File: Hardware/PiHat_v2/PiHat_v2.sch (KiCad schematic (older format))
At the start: 35 parts, among them P1 RPiGPIO, P2 CONN_01X02, P3 CONN_01X08

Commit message: KiCad Closeout Updates
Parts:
- renumbered aux1 to ADC6, aux3 to GPIO20, aux4 to GPIO21, aux5 to GPIO26, S1 to PB1, aux2 to PD3
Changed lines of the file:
@@
 $EndComp
 $Comp
-L Piezo S1
+L Piezo PB1
 U 1 1 5889681E
 P 6000 5100
-F 0 "S1" H 6000 5250 50  0000 C CNN
+F 0 "PB1" H 6000 5250 50  0000 C CNN
 F 1 "Piezo" V 6100 5100 50  0000 C CNN
 F 2 ".pretty:Piezo_CT-1205h-smt" H 6000 5100 50  0001 C CNN
@@
 	4450 1050 4450 1250
 $Comp
-L aux_conn aux1
+L aux_conn ADC6
 U 1 1 5946D2A9
 P 6050 5850
-F 0 "aux1" H 6050 6000 50  0000 C CNN
+F 0 "ADC6" H 6050 6000 50  0000 C CNN
 F 1 "aux_conn" V 6150 5850 50  0000 C CNN
 F 2 ".pretty:Pin_Header_Straight_1x02_Pitch2.54mm" H 6050 5850 50  0001 C CNN
@@
 $EndComp
 $Comp
-L aux_conn aux2
+L aux_conn PD3
 U 1 1 5946D408
 P 6050 6200
-F 0 "aux2" H 6050 6350 50  0000 C CNN
+F 0 "PD3" H 6050 6350 50  0000 C CNN
 F 1 "aux_conn" V 6150 6200 50  0000 C CNN
 F 2 ".pretty:Pin_Header_Straight_1x02_Pitch2.54mm" H 6050 6200 50  0001 C CNN
@@
 $EndComp
 $Comp
-L aux_conn aux3
+L aux_conn GPIO20
 U 1 1 5946D47A
 P 6050 6550
-F 0 "aux3" H 6050 6700 50  0000 C CNN
+F 0 "GPIO20" H 6050 6700 50  0000 C CNN
 F 1 "aux_conn" V 6150 6550 50  0000 C CNN
 F 2 ".pretty:Pin_Header_Straight_1x02_Pitch2.54mm" H 6050 6550 50  0001 C CNN
@@
 $EndComp
 $Comp
-L aux_conn aux4
+L aux_conn GPIO21
 U 1 1 5946D4EB
 P 6050 6900
-F 0 "aux4" H 6050 7050 50  0000 C CNN
+F 0 "GPIO21" H 6050 7050 50  0000 C CNN
 F 1 "aux_conn" V 6150 6900 50  0000 C CNN
 F 2 ".pretty:Pin_Header_Straight_1x02_Pitch2.54mm" H 6050 6900 50  0001 C CNN
@@
 $EndComp
 $Comp
-L aux_conn aux5
+L aux_conn GPIO26
 U 1 1 5946D55F
 P 6050 7250
-F 0 "aux5" H 6050 7400 50  0000 C CNN
+F 0 "GPIO26" H 6050 7400 50  0000 C CNN
 F 1 "aux_conn" V 6150 7250 50  0000 C CNN
 F 2 ".pretty:Pin_Header_Straight_1x02_Pitch2.54mm" H 6050 7250 50  0001 C CNN

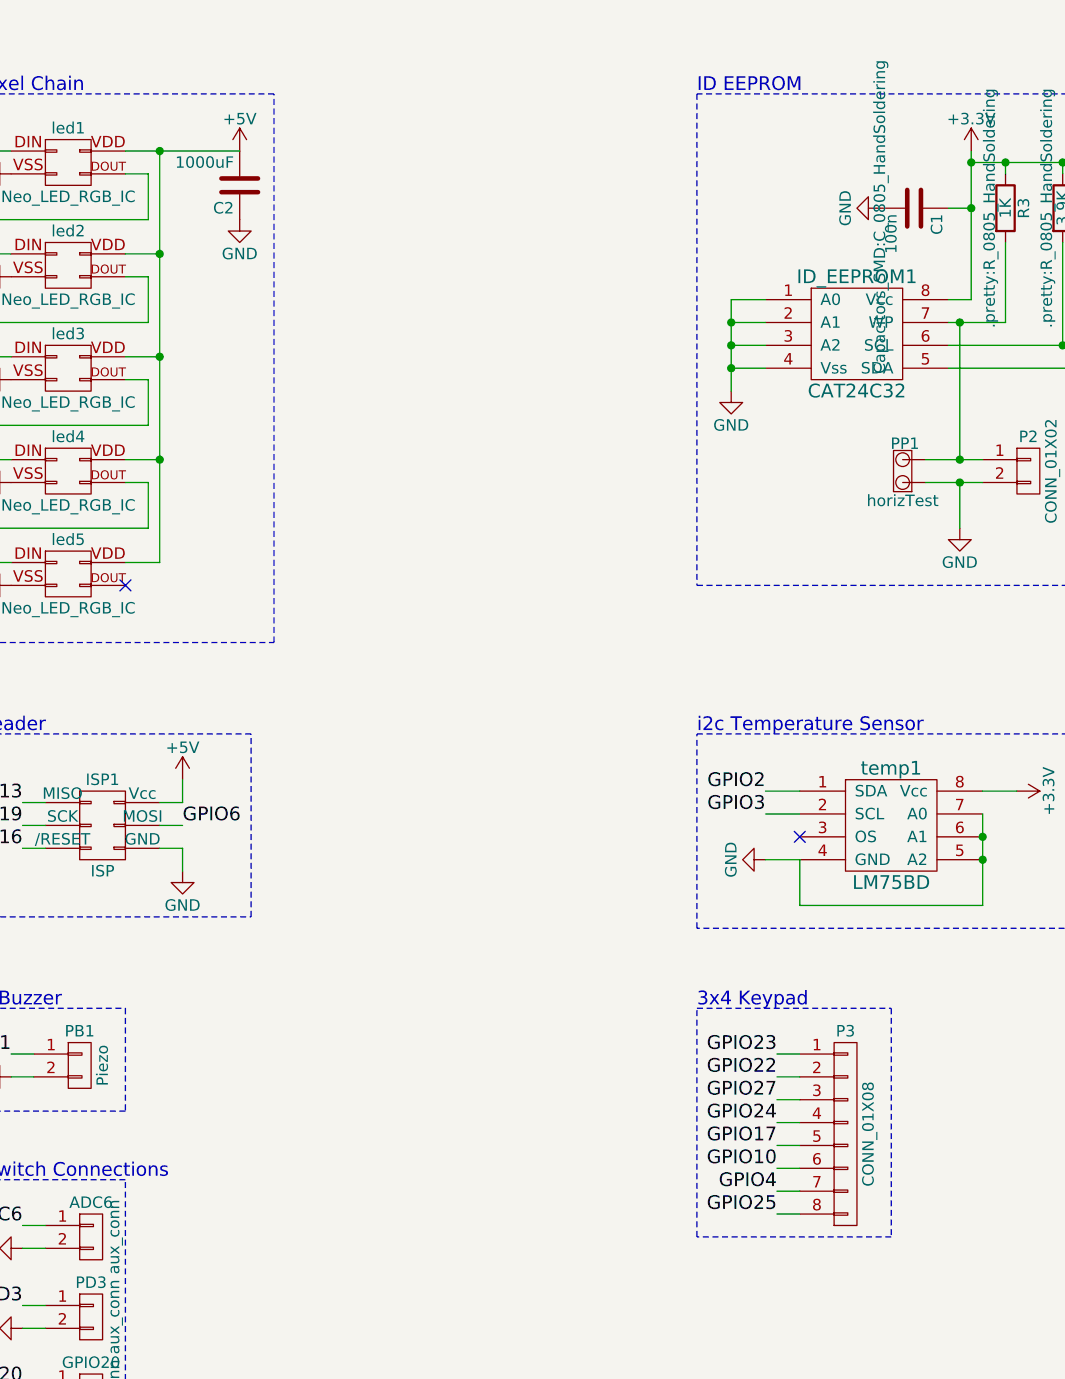
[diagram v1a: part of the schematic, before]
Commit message: Pi Hat - now with non-imaginary components (#155)
* Adjust Silkscreen Layout on PCB

* Add 1000uF AluCap Footprint & Rename 100nF to 0.1uF

* Implement AluCap in PCB

* Connect New Keypad GPIO Schema

* Built the BOM

* Move Silkscreen Logo

* YASA - Yet Another Silkscreen Adjustment

* Update Version Number of PiHat

* Rotate AluCap for Proper Polarity

* Fix BOM Whitespace
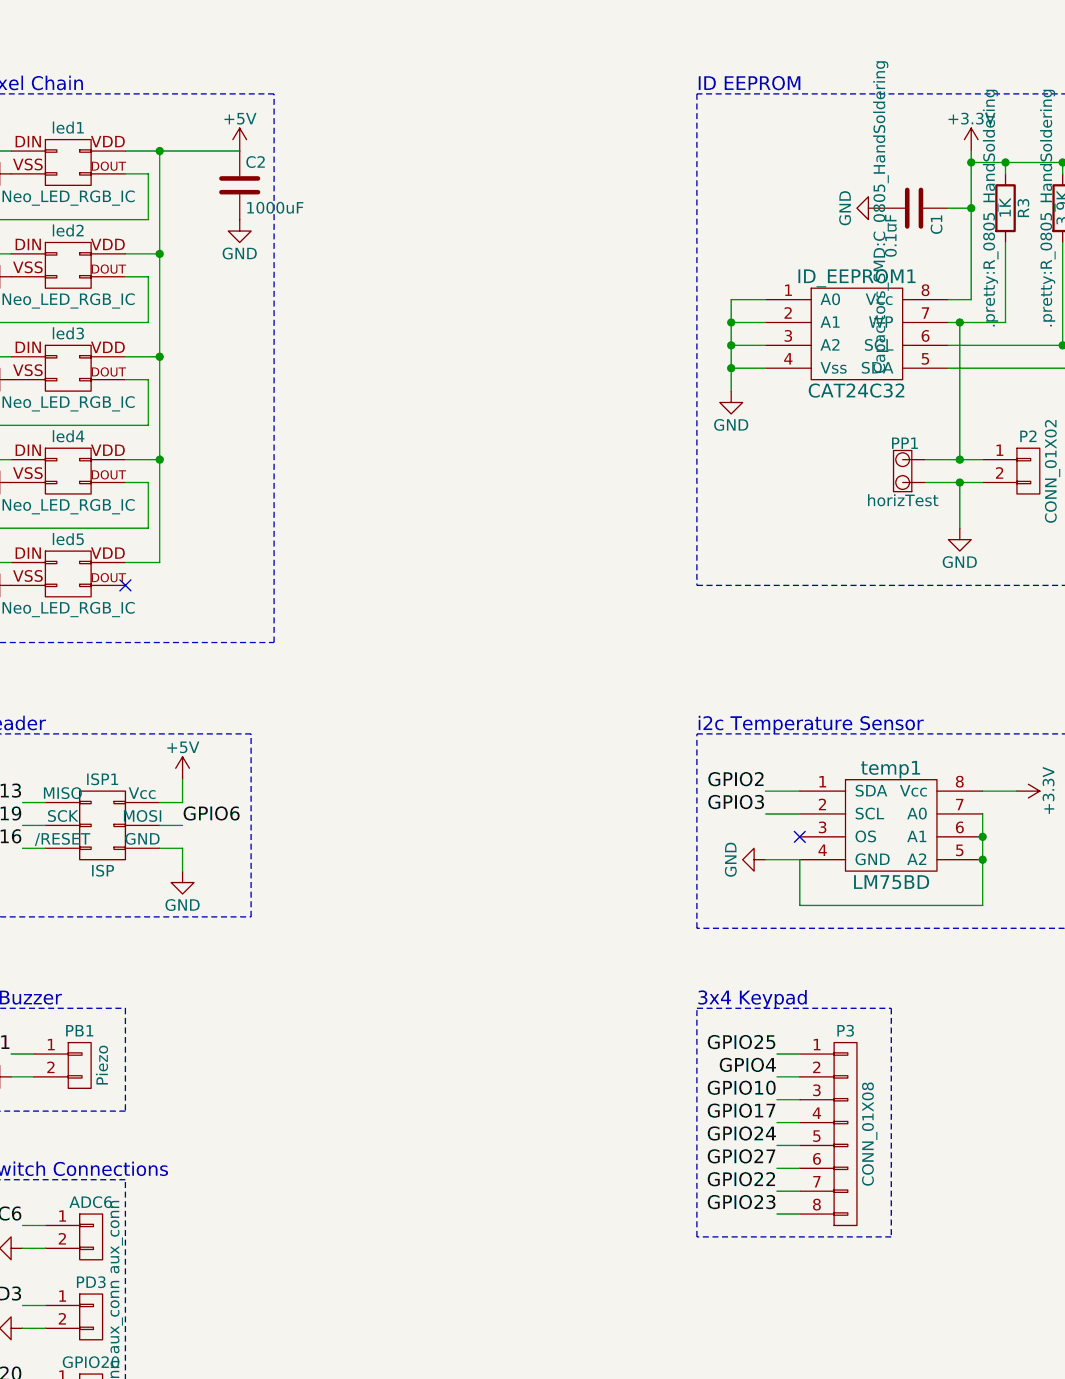
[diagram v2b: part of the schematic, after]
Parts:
- C1: value 100n -> 0.1uF
- C2: footprint Capacitors_SMD:C_0805_HandSoldering -> .pretty:AluCap_8mmDia_Nichicon
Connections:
- net +5V: now also C2.1; no longer C2.2
- net GND: now also C2.2; no longer C2.1
- net GPIO10: now also P3.3 (P3); no longer P3.6 (P6)
- net GPIO17: now also P3.4 (P4); no longer P3.5 (P5)
- net GPIO22: now also P3.7 (P7); no longer P3.2 (P2)
- net GPIO23: now also P3.8 (P8); no longer P3.1 (P1)
- net GPIO24: now also P3.5 (P5); no longer P3.4 (P4)
- net GPIO25: now also P3.1 (P1); no longer P3.8 (P8)
- net GPIO27: now also P3.6 (P6); no longer P3.3 (P3)
- net GPIO4: now also P3.2 (P2); no longer P3.7 (P7)
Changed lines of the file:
@@
 P 9650 1350
 F 0 "C1" H 9675 1450 50  0000 L CNN
-F 1 "100n" H 9675 1250 50  0000 L CNN
+F 1 "0.1uF" H 9675 1250 50  0000 L CNN
 F 2 "Capacitors_SMD:C_0805_HandSoldering" H 9688 1200 50  0000 C CNN
 F 3 "" H 9650 1350 50  0000 C CNN
@@
 F 0 "C2" H 6725 1350 50  0000 L CNN
 F 1 "1000uF" H 6725 1150 50  0000 L CNN
-F 2 "Capacitors_SMD:C_0805_HandSoldering" H 6738 1100 50  0001 C CNN
+F 2 ".pretty:AluCap_8mmDia_Nichicon" H 6738 1100 50  0001 C CNN
 F 3 "" H 6700 1250 50  0000 C CNN
 	1    6700 1250
-	-1   0    0    1
+	1    0    0    -1
 $EndComp
 $Comp
@@
 Text Label 5700 5050 2    60   ~ 0
 PB1
+Text Label 9050 5150 2    60   ~ 0
+GPIO4
+Text Label 9050 5350 2    60   ~ 0
+GPIO17
+Text Label 9050 5550 2    60   ~ 0
+GPIO27
+Text Label 9050 5750 2    60   ~ 0
+GPIO23
 Text Label 9050 5650 2    60   ~ 0
-GPIO4
+GPIO22
 Text Label 9050 5450 2    60   ~ 0
-GPIO17
+GPIO24
 Text Label 9050 5250 2    60   ~ 0
-GPIO27
+GPIO10
 Text Label 9050 5050 2    60   ~ 0
-GPIO23
-Text Label 9050 5150 2    60   ~ 0
-GPIO22
-Text Label 9050 5350 2    60   ~ 0
-GPIO24
-Text Label 9050 5550 2    60   ~ 0
-GPIO10
-Text Label 9050 5750 2    60   ~ 0
 GPIO25
 $Comp

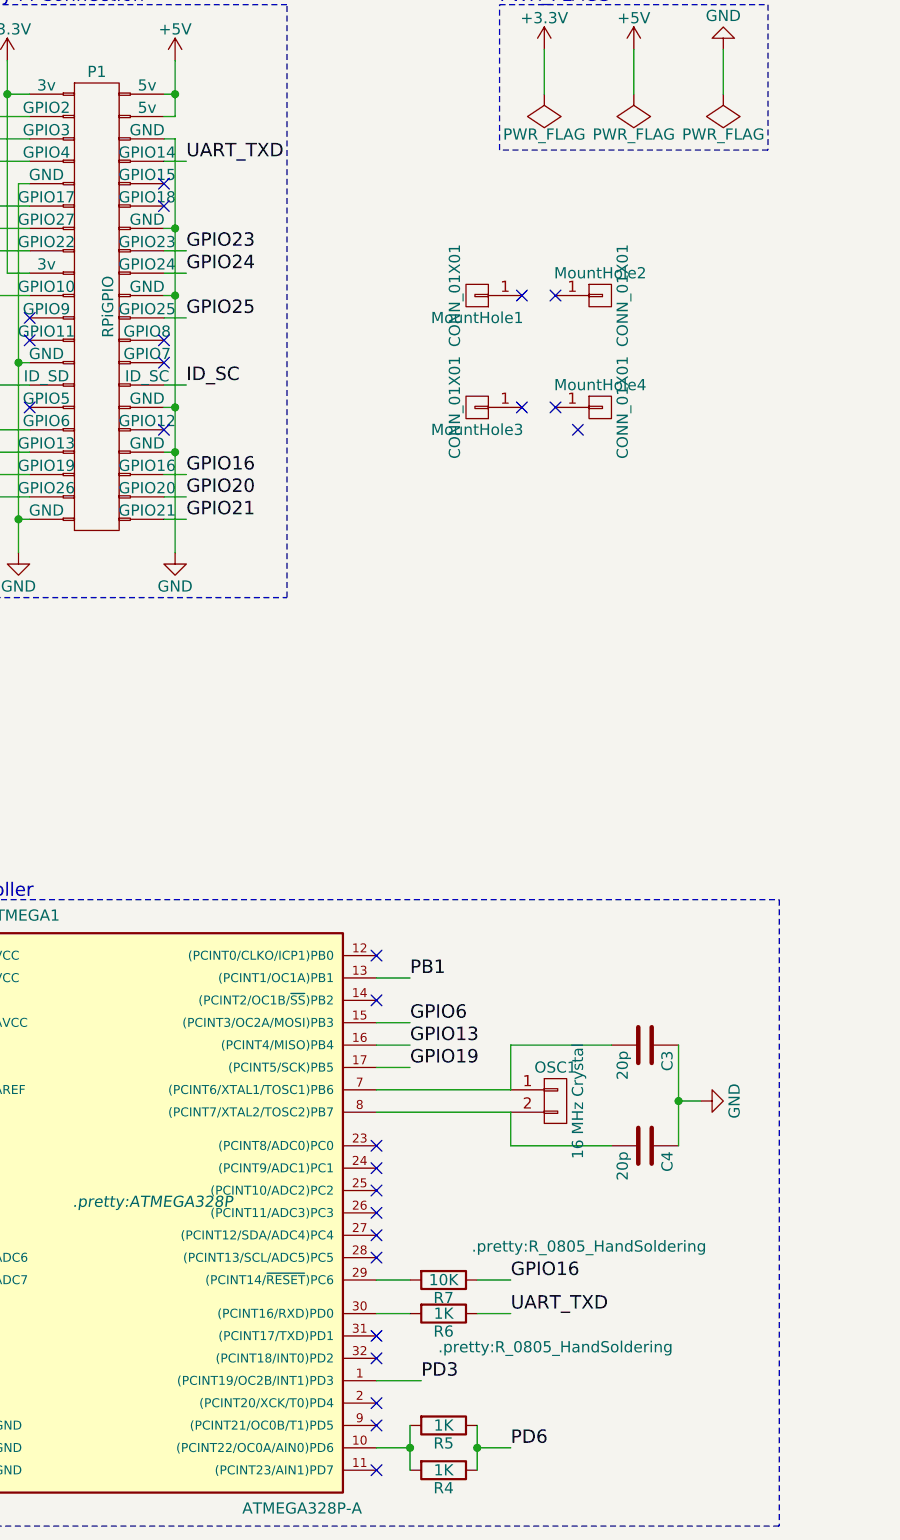
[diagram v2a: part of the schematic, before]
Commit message: Connect GPIO RX and ATMega TX - Enlarge select silkscreen graphics
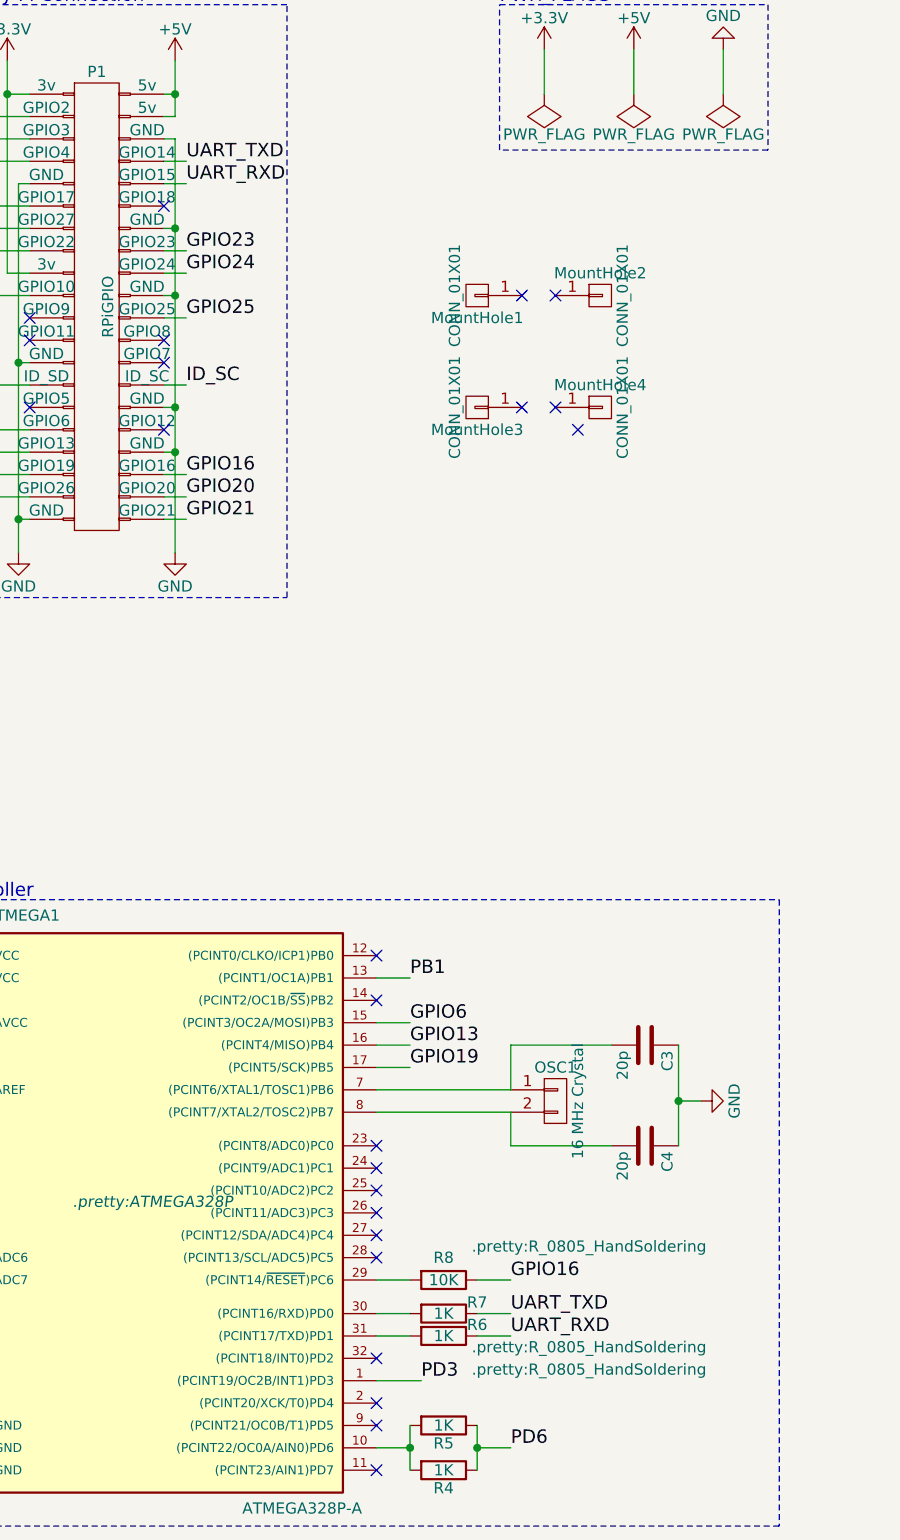
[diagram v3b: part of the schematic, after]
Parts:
- added R6: 1K, .pretty:R_0805_HandSoldering, symbol R
- renumbered R6 to R7, R7 to R8
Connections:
- net at ATMEGA1.31 ((PCINT17/TXD)PD1): now also R6.2
- net UART_RXD: now reaches P1.10 (GPIO15)
- net UART_RXD: now also R6.1
- no-connect marks 30 -> 28
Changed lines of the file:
@@
 UART_TXD
 $Comp
-L R R6
+L R R7
 U 1 1 5927814D
 P 3200 6700
-F 0 "R6" V 3280 6700 50  0000 C CNN
+F 0 "R7" V 3150 6850 50  0000 C CNN
 F 1 "1K" V 3200 6700 50  0000 C CNN
-F 2 ".pretty:R_0805_HandSoldering" V 3350 7200 50  0000 C CNN
+F 2 ".pretty:R_0805_HandSoldering" V 3350 7350 50  0000 C CNN
 F 3 "" H 3200 6700 50  0000 C CNN
 F 4 "1%" V 3200 6700 60  0001 C CNN "Tolerance"
@@
 Microcontroller\n
 $Comp
-L R R7
+L R R8
 U 1 1 592A1176
 P 3200 6550
-F 0 "R7" V 3280 6550 50  0000 C CNN
+F 0 "R8" V 3100 6550 50  0000 C CNN
 F 1 "10K" V 3200 6550 50  0000 C CNN
 F 2 ".pretty:R_0805_HandSoldering" V 3050 7200 50  0000 C CNN
@@
 NoConn ~ 1950 2350
 NoConn ~ 1950 1750
-NoConn ~ 1950 1650
 NoConn ~ 2900 5950
 NoConn ~ 2900 6050
@@
 NoConn ~ 2900 6350
 NoConn ~ 2900 6450
-NoConn ~ 2900 6800
 NoConn ~ 2900 6900
 NoConn ~ 2900 7100
@@
 NoConn ~ 3550 2650
 NoConn ~ 3800 2750
+$Comp
+L R R6
+U 1 1 595347C0
+P 3200 6800
+F 0 "R6" V 3150 6950 50  0000 C CNN
+F 1 "1K" V 3200 6800 50  0000 C CNN
+F 2 ".pretty:R_0805_HandSoldering" V 3350 7450 50  0000 C CNN
+F 3 "" H 3200 6800 50  0000 C CNN
+F 4 "1%" V 3200 6800 60  0001 C CNN "Tolerance"
+	1    3200 6800
+	0    1    1    0
+$EndComp
+Wire Wire Line
+	3350 6800 3500 6800
+Text Label 3500 6800 0    60   ~ 0
+UART_RXD
+Wire Wire Line
+	1950 1650 2050 1650
+Text Label 2050 1650 0    60   ~ 0
+UART_RXD
+Wire Wire Line
+	2900 6800 3050 6800
 $EndSCHEMATC
